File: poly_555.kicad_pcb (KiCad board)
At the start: 2 copper layers, 114.3 x 141 mm, 162 parts, among them U1 LM386, U10 555, U11 555, U12 555, U13 555, U14 555, U2 555, U3 555, U4 555, U5 555, U6 555, U7 555, U8 555, U9 555

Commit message: Routed and error-free
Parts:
- BT1: value 9v -> +
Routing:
- net /sheet5EF259DC/9v: track 41.2 -> 160.5 mm, vias 0 -> 3
- net /sheet5EF2B20E/9v: track 41.2 -> 158.2 mm, vias 0 -> 3
- net /sheet5EF60550/9v: track 41.2 -> 151.3 mm, vias 0 -> 3
- net /sheet5EF17814/9v: track 41.2 -> 149.2 mm
- net /sheet5EF27E47/9v: track 41.2 -> 138.3 mm, vias 0 -> 4
- net /sheet5EF2302B/9v: track 41.2 -> 128.2 mm, vias 0 -> 1
- net /555_astable/9v: track 41.2 -> 123.2 mm
- net /sheet5EF60552/9v: track 41.2 -> 115.4 mm
- net /sheet5EF60554/9v: track 41.2 -> 101.5 mm
- net Net-(BT1-Pad1): track 343.5 -> 397.5 mm
- net /sheet5EF60551/9v: track 41.2 -> 95.1 mm
- net /sheet5EF60553/9v: track 41.2 -> 85.4 mm
- net /sheet5EF60555/9v: track 41.2 -> 73.4 mm
- net /sheet5EF7A07A/9v: track 41.2 -> 70.7 mm
- net /555_astable/Out: track 322.1 -> 348.2 mm
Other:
- board text added: "9V"
- board text added: "FINE COURSE"
- board text added: "SPEAKER"
- board text added: "VOLUME"

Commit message: Tracks copied over, TEMP
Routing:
- net (no net): track 0.00 -> 893.6 mm
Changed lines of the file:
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@@
     (thickness 1.6)
     (drawings 24)
-    (tracks 875)
+    (tracks 960)
     (zones 0)
     (modules 162)
@@
   (page A4)
   (layers
-    (0 F.Cu signal hide)
-    (31 B.Cu signal hide)
+    (0 F.Cu signal)
+    (31 B.Cu signal)
     (32 B.Adhes user)
     (33 F.Adhes user)
@@
     (effects (font (size 1 1) (thickness 0.15)))
   )
+  (segment (start 179.822 89.154) (end 163.648 105.328) (width 0.6969) (layer F.Cu) (net 0))
+  (segment (start 163.648 105.328) (end 163.648 164.465) (width 0.6969) (layer F.Cu) (net 0))
+  (segment (start 171.268 159.385) (end 168.09699 156.21399) (width 0.6969) (layer F.Cu) (net 0))
+  (segment (start 186.722001 87.104001) (end 190.181501 83.644501) (width 0.6969) (layer F.Cu) (net 0))
+  (segment (start 168.09699 105.489008) (end 186.481997 87.104001) (width 0.6969) (layer F.Cu) (net 0))
+  (segment (start 190.181501 63.499001) (end 189.1565 62.474) (width 0.6969) (layer F.Cu) (net 0))
+  (segment (start 190.181501 83.644501) (end 190.181501 63.499001) (width 0.6969) (layer F.Cu) (net 0))
+  (segment (start 168.09699 156.21399) (end 168.09699 105.489008) (width 0.6969) (layer F.Cu) (net 0))
+  (segment (start 191.897 136.521998) (end 178.888 149.530998) (width 0.6969) (layer F.Cu) (net 0))
+  (segment (start 196.342 120.904) (end 191.897 125.349) (width 0.6969) (layer F.Cu) (net 0))
+  (segment (start 178.888 149.530998) (end 178.888 164.465) (width 0.6969) (layer F.Cu) (net 0))
+  (segment (start 198.102001 119.143999) (end 196.342 120.904) (width 0.6969) (layer F.Cu) (net 0))
+  (segment (start 198.102001 97.797999) (end 198.102001 119.143999) (width 0.6969) (layer F.Cu) (net 0))
+  (segment (start 206.8095 89.0905) (end 198.102001 97.797999) (width 0.6969) (layer F.Cu) (net 0))
+  (segment (start 191.897 125.349) (end 191.897 136.521998) (width 0.6969) (layer F.Cu) (net 0))
+  (segment (start 217.296001 64.521999) (end 217.296001 90.281001) (width 0.6969) (layer F.Cu) (net 0))
+  (segment (start 216.271 62.474) (end 216.271 63.496998) (width 0.6969) (layer F.Cu) (net 0))
+  (segment (start 217.296001 90.281001) (end 213.978002 93.599) (width 0.6969) (layer F.Cu) (net 0))
+  (segment (start 216.271 63.496998) (end 217.296001 64.521999) (width 0.6969) (layer F.Cu) (net 0))
+  (segment (start 209.677 93.599) (end 207.164998 93.599) (width 0.6969) (layer F.Cu) (net 0))
+  (segment (start 200.787 120.269) (end 200.787 118.364) (width 0.6969) (layer F.Cu) (net 0))
+  (segment (start 207.164998 93.599) (end 204.597 93.599) (width 0.6969) (layer F.Cu) (net 0))
+  (segment (start 200.787 123.860002) (end 200.787 120.269) (width 0.6969) (layer F.Cu) (net 0))
+  (segment (start 213.978002 93.599) (end 212.329998 93.599) (width 0.6969) (layer F.Cu) (net 0))
+  (segment (start 212.329998 93.599) (end 209.677 93.599) (width 0.6969) (layer F.Cu) (net 0))
+  (segment (start 197.021999 124.669001) (end 199.978001 124.669001) (width 0.6969) (layer F.Cu) (net 0))
+  (segment (start 200.387001 97.808999) (end 204.597 93.599) (width 0.6969) (layer F.Cu) (net 0))
+  (segment (start 200.387001 117.964001) (end 200.387001 97.808999) (width 0.6969) (layer F.Cu) (net 0))
+  (segment (start 199.978001 124.669001) (end 200.787 123.860002) (width 0.6969) (layer F.Cu) (net 0))
+  (segment (start 195.274989 137.211011) (end 195.274989 126.416011) (width 0.6969) (layer F.Cu) (net 0))
+  (segment (start 188.966999 143.519001) (end 195.274989 137.211011) (width 0.6969) (layer F.Cu) (net 0))
+  (segment (start 195.274989 126.416011) (end 197.021999 124.669001) (width 0.6969) (layer F.Cu) (net 0))
+  (segment (start 187.439997 143.519001) (end 188.966999 143.519001) (width 0.6969) (layer F.Cu) (net 0))
+  (segment (start 185.658001 145.300997) (end 187.439997 143.519001) (width 0.6969) (layer F.Cu) (net 0))
+  (segment (start 185.658001 158.535001) (end 185.658001 145.300997) (width 0.6969) (layer F.Cu) (net 0))
+  (segment (start 210.947 156.464) (end 206.850999 160.560001) (width 0.6969) (layer F.Cu) (net 0))
+  (segment (start 206.850999 160.560001) (end 204.597 162.814) (width 0.6969) (layer F.Cu) (net 0))
+  (segment (start 223.647 121.539) (end 217.932 127.254) (width 0.6969) (layer F.Cu) (net 0))
+  (segment (start 217.932 127.254) (end 217.932 144.399) (width 0.6969) (layer F.Cu) (net 0))
+  (segment (start 204.597 162.814) (end 195.779 162.814) (width 0.6969) (layer F.Cu) (net 0))
+  (segment (start 195.779 162.814) (end 194.128 164.465) (width 0.6969) (layer F.Cu) (net 0))
+  (segment (start 210.947 154.362002) (end 210.947 156.464) (width 0.6969) (layer F.Cu) (net 0))
+  (segment (start 232.130001 113.055999) (end 223.647 121.539) (width 0.6969) (layer F.Cu) (net 0))
+  (segment (start 217.932 144.399) (end 217.932 147.377002) (width 0.6969) (layer F.Cu) (net 0))
+  (segment (start 217.932 147.377002) (end 210.947 154.362002) (width 0.6969) (layer F.Cu) (net 0))
+  (segment (start 234.178 89.154) (end 232.130001 91.201999) (width 0.6969) (layer F.Cu) (net 0))
+  (segment (start 232.130001 91.201999) (end 232.130001 113.055999) (width 0.6969) (layer F.Cu) (net 0))
+  (segment (start 255.397 105.029) (end 255.397 117.375998) (width 0.6969) (layer F.Cu) (net 0))
+  (segment (start 255.397 117.375998) (end 248.412 124.360998) (width 0.6969) (layer F.Cu) (net 0))
+  (segment (start 248.412 124.360998) (end 248.412 147.574) (width 0.6969) (layer F.Cu) (net 0))
+  (segment (start 248.412 147.574) (end 243.411999 152.574001) (width 0.6969) (layer F.Cu) (net 0))
+  (segment (start 243.411999 152.574001) (end 221.258999 152.574001) (width 0.6969) (layer F.Cu) (net 0))
+  (segment (start 221.258999 152.574001) (end 209.368 164.465) (width 0.6969) (layer F.Cu) (net 0))
+  (segment (start 261.864 89.154) (end 260.838999 90.179001) (width 0.6969) (layer F.Cu) (net 0))
+  (segment (start 260.838999 90.179001) (end 260.838999 97.047001) (width 0.6969) (layer F.Cu) (net 0))
+  (segment (start 260.838999 97.047001) (end 255.397 102.489) (width 0.6969) (layer F.Cu) (net 0))
+  (segment (start 255.397 102.489) (end 255.397 105.029) (width 0.6969) (layer F.Cu) (net 0))
+  (segment (start 224.608 164.465) (end 218.352999 158.209999) (width 0.6969) (layer F.Cu) (net 0))
+  (segment (start 218.352999 158.209999) (end 195.537999 158.209999) (width 0.6969) (layer F.Cu) (net 0))
+  (segment (start 195.537999 158.209999) (end 179.822 142.494) (width 0.6969) (layer F.Cu) (net 0))
+  (segment (start 230.602989 157.759989) (end 232.228 159.385) (width 0.6969) (layer F.Cu) (net 0))
+  (segment (start 189.347 115.824) (end 190.046999 116.523999) (width 0.6969) (layer F.Cu) (net 0))
+  (segment (start 195.072 142.897602) (end 209.934387 157.759989) (width 0.6969) (layer F.Cu) (net 0))
+  (segment (start 190.046999 116.523999) (end 190.046999 117.546997) (width 0.6969) (layer F.Cu) (net 0))
+  (segment (start 190.046999 117.546997) (end 195.072 122.571998) (width 0.6969) (layer F.Cu) (net 0))
+  (segment (start 195.072 122.571998) (end 195.072 142.897602) (width 0.6969) (layer F.Cu) (net 0))
+  (segment (start 209.934387 157.759989) (end 230.602989 157.759989) (width 0.6969) (layer F.Cu) (net 0))
+  (segment (start 239.848 164.465) (end 239.848 160.765998) (width 0.6969) (layer F.Cu) (net 0))
+  (segment (start 208.025001 143.519001) (end 207 142.494) (width 0.6969) (layer F.Cu) (net 0))
+  (segment (start 222.601003 143.519001) (end 208.025001 143.519001) (width 0.6969) (layer F.Cu) (net 0))
+  (segment (start 239.848 160.765998) (end 222.601003 143.519001) (width 0.6969) (layer F.Cu) (net 0))
+  (segment (start 240.8274 159.385) (end 225.073001 143.630601) (width 0.6969) (layer F.Cu) (net 0))
+  (segment (start 217.550001 132.482603) (end 217.550001 117.602411) (width 0.6969) (layer F.Cu) (net 0))
+  (segment (start 247.468 159.385) (end 240.8274 159.385) (width 0.6969) (layer F.Cu) (net 0))
+  (segment (start 225.073001 140.005603) (end 217.550001 132.482603) (width 0.6969) (layer F.Cu) (net 0))
+  (segment (start 217.550001 117.602411) (end 216.525 116.57741) (width 0.6969) (layer F.Cu) (net 0))
+  (segment (start 225.073001 143.630601) (end 225.073001 140.005603) (width 0.6969) (layer F.Cu) (net 0))
+  (segment (start 238.331001 144.008999) (end 255.088 160.765998) (width 0.6969) (layer F.Cu) (net 0))
+  (segment (start 235.692999 144.008999) (end 238.331001 144.008999) (width 0.6969) (layer F.Cu) (net 0))
+  (segment (start 255.088 160.765998) (end 255.088 164.465) (width 0.6969) (layer F.Cu) (net 0))
+  (segment (start 234.178 142.494) (end 235.692999 144.008999) (width 0.6969) (layer F.Cu) (net 0))
+  (segment (start 269.486003 143.519001) (end 262.889001 143.519001) (width 0.6969) (layer F.Cu) (net 0))
+  (segment (start 270.509001 164.283999) (end 270.509001 144.541999) (width 0.6969) (layer F.Cu) (net 0))
+  (segment (start 270.509001 144.541999) (end 269.486003 143.519001) (width 0.6969) (layer F.Cu) (net 0))
+  (segment (start 262.889001 143.519001) (end 261.864 142.494) (width 0.6969) (layer F.Cu) (net 0))
   (segment (start 53.180999 178.236001) (end 54.356 177.061) (width 0.25) (layer B.Cu) (net 1) (status 20))
   (segment (start 40.291001 178.236001) (end 53.180999 178.236001) (width 0.25) (layer B.Cu) (net 1))

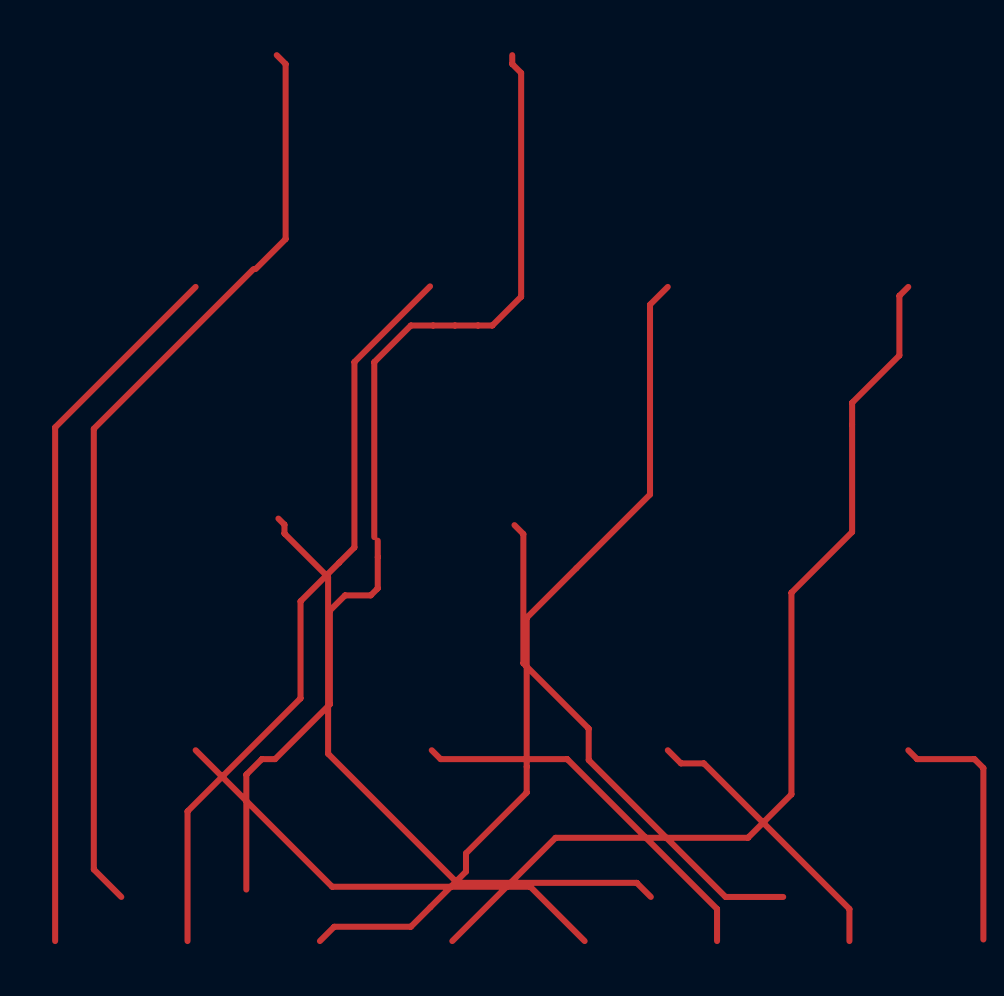
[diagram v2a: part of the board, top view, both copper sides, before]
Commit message: Track copies as silkscreen
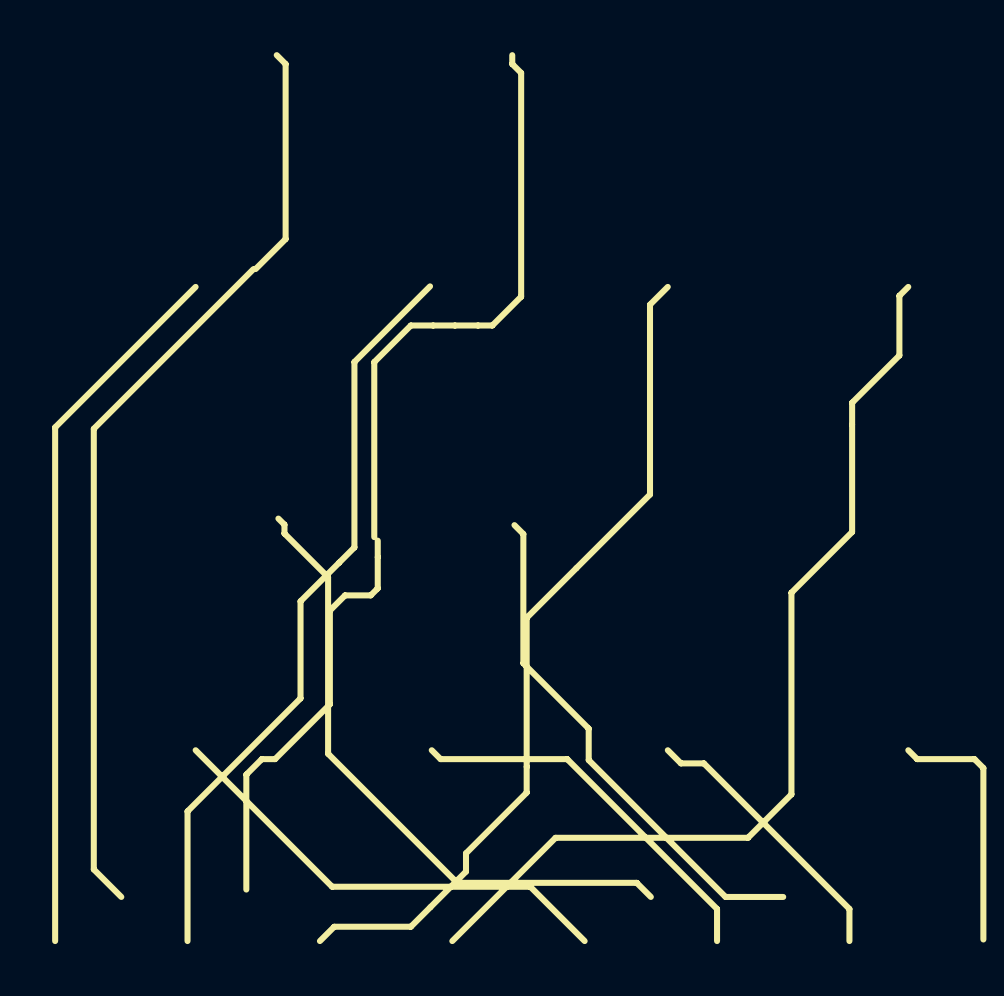
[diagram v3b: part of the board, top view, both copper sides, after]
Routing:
- net (no net): track 893.6 -> 0.00 mm

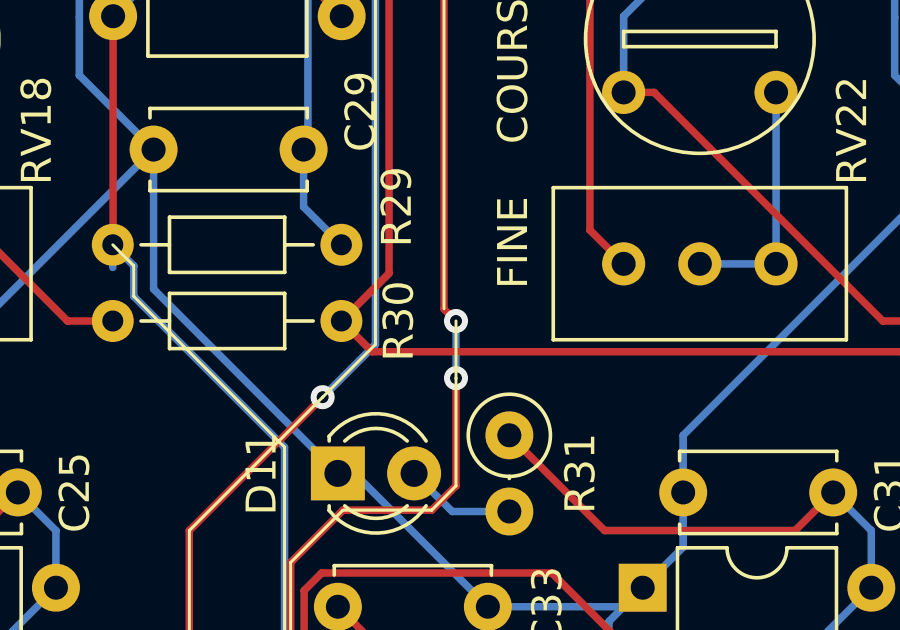
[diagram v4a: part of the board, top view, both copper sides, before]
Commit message: Connect via'd silkscreen track
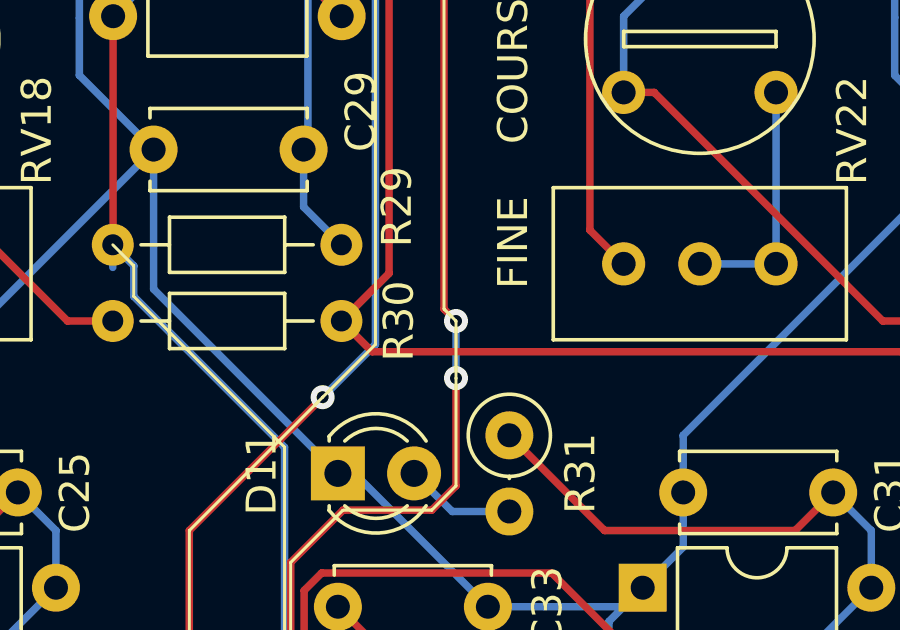
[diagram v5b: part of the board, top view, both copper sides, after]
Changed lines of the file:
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@@
   (general
     (thickness 1.6)
-    (drawings 109)
+    (drawings 110)
     (tracks 875)
     (zones 0)
@@
     )
   )
+  (gr_line (start 71.355001 124.060001) (end 71.755 124.46) (layer F.SilkS) (width 0.1))
   (gr_line (start 50.79 95.25) (end 34.616 111.424) (layer F.SilkS) (width 0.1))
   (gr_line (start 34.616 111.424) (end 34.616 170.561) (layer F.SilkS) (width 0.1))

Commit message: Align PCB to 0,0
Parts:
- removed the REF** at (90.2, 181.0)
- removed the REF** at (143.5, 181.0)
- removed the REF** at (36.8, 181.0)
- removed the REF** at (143.5, 47.6)
- added REF**: MountingHole_3.2mm_M3, MountingHole:MountingHole_3.2mm_M3, F.Cu at (57.1, -3.81)
- added REF**: MountingHole_3.2mm_M3, MountingHole:MountingHole_3.2mm_M3, F.Cu at (110.5, -3.81)
- added REF**: MountingHole_3.2mm_M3, MountingHole:MountingHole_3.2mm_M3, F.Cu at (3.81, -3.81)
- added REF**: MountingHole_3.2mm_M3, MountingHole:MountingHole_3.2mm_M3, F.Cu at (110.5, -137.2)
- moved C12 187.7 mm to (34.6, -104.2)
- moved C25 187.7 mm to (24.1, -54.6)
- moved C27 187.7 mm to (7.62, -50.8)
- moved C29 187.7 mm to (33.7, -66.0)
- moved C31 187.7 mm to (51.3, -54.6)
- moved C33 187.7 mm to (34.8, -50.8)
- moved C35 187.7 mm to (60.8, -66.0)
- moved C37 187.7 mm to (78.5, -54.6)
- moved C39 187.7 mm to (62.0, -50.8)
- moved C40 187.7 mm to (106.2, -54.6)
- moved C42 187.7 mm to (89.7, -50.8)
- moved D10 187.7 mm to (17.1, -81.9)
- moved D12 187.7 mm to (44.3, -81.9)
- moved R16 187.7 mm to (67.7, -109.9)
- moved R18 187.7 mm to (79.7, -87.0)
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
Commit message: Add TODO about uneven PCB top line
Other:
- board text added: "TODO: uneven top line"
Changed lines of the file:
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@@
   (general
     (thickness 1.6)
-    (drawings 110)
+    (drawings 111)
     (tracks 875)
     (zones 0)
@@
     )
   )
+  (gr_text "TODO: uneven top line" (at 34.798 -143.51) (layer Cmts.User)
+    (effects (font (size 1.5 1.5) (thickness 0.3)))
+  )
   (gr_line (start 38.335001 -60.724999) (end 38.735 -60.325) (layer F.SilkS) (width 0.1))
